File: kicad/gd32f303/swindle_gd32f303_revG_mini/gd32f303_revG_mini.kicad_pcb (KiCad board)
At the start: 2 copper layers, 39.3 x 30.1 mm, 55 parts, among them J1 Debug port, J2 Debug port, J3 USB, J40 J40, J7 Conn_01x05_Pin, Q1 DMG2302U, U1 GD32F303, U5 LM1117-3.3, Y2 8Mhz

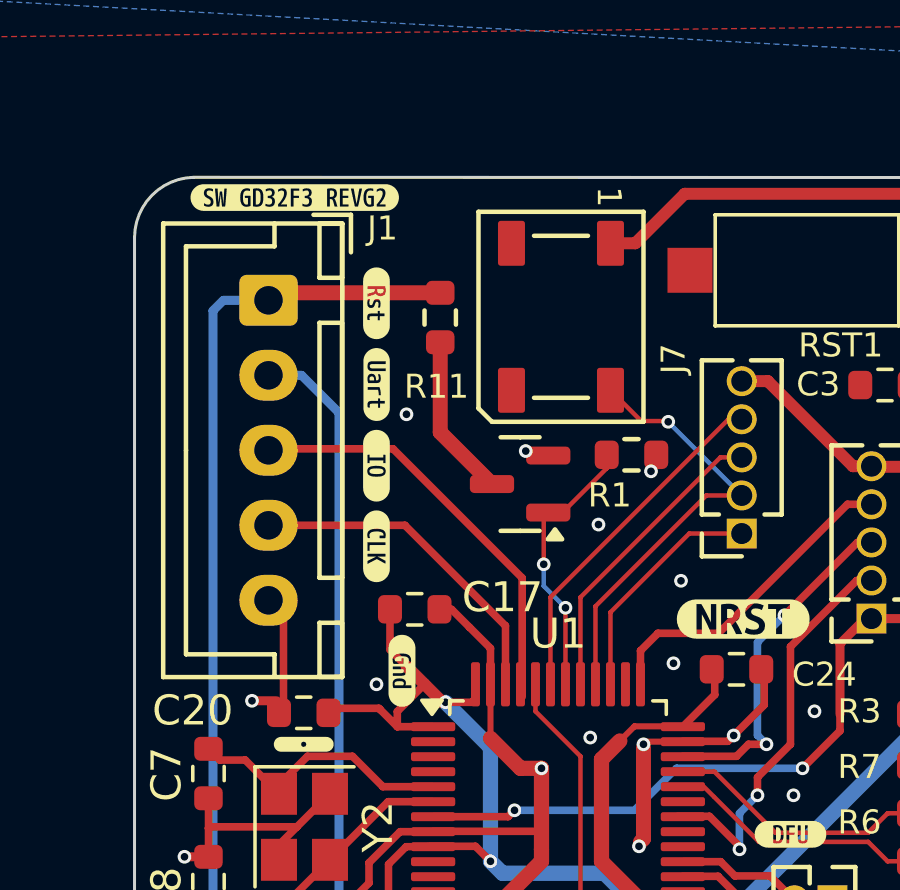
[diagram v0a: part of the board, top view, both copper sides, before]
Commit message: kicad: add pullup resistor on GD32/48 version
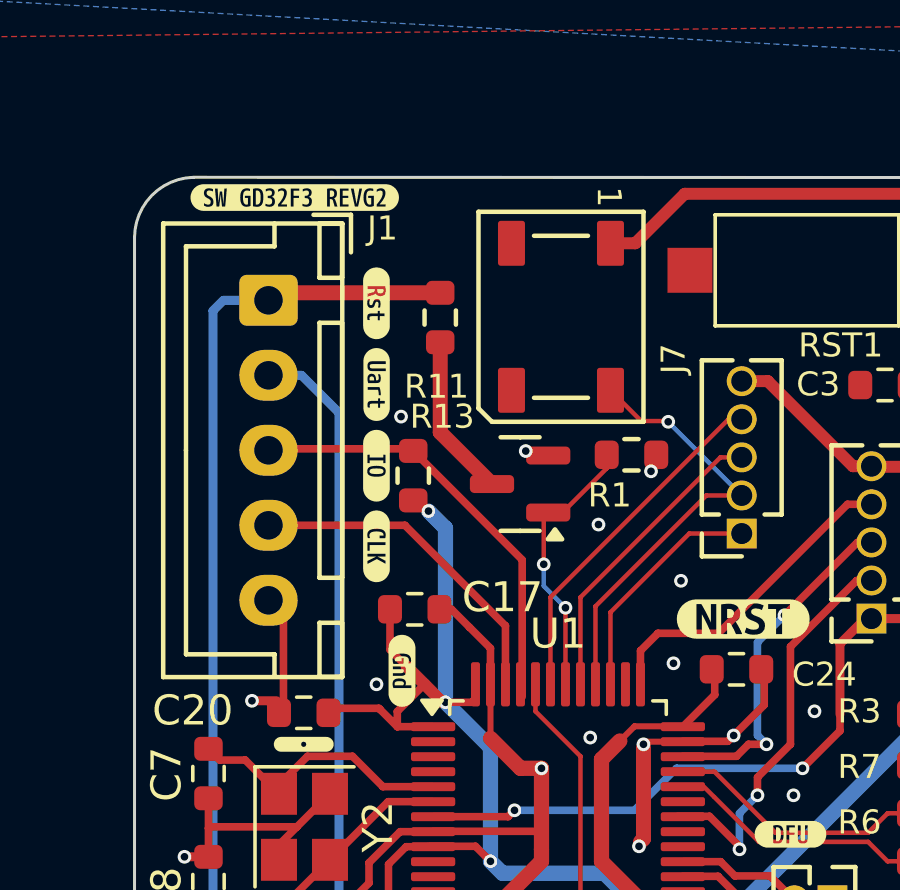
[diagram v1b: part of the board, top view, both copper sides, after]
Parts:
- added R13: 1k, Resistor_SMD:R_0603_1608Metric, F.Cu at (125.4, 79.8)
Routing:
- net +3.3V: track 90.4 -> 97.0 mm, vias 7 -> 8
